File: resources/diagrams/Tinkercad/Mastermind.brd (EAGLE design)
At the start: 68.6 x 53.3 mm, 4 parts

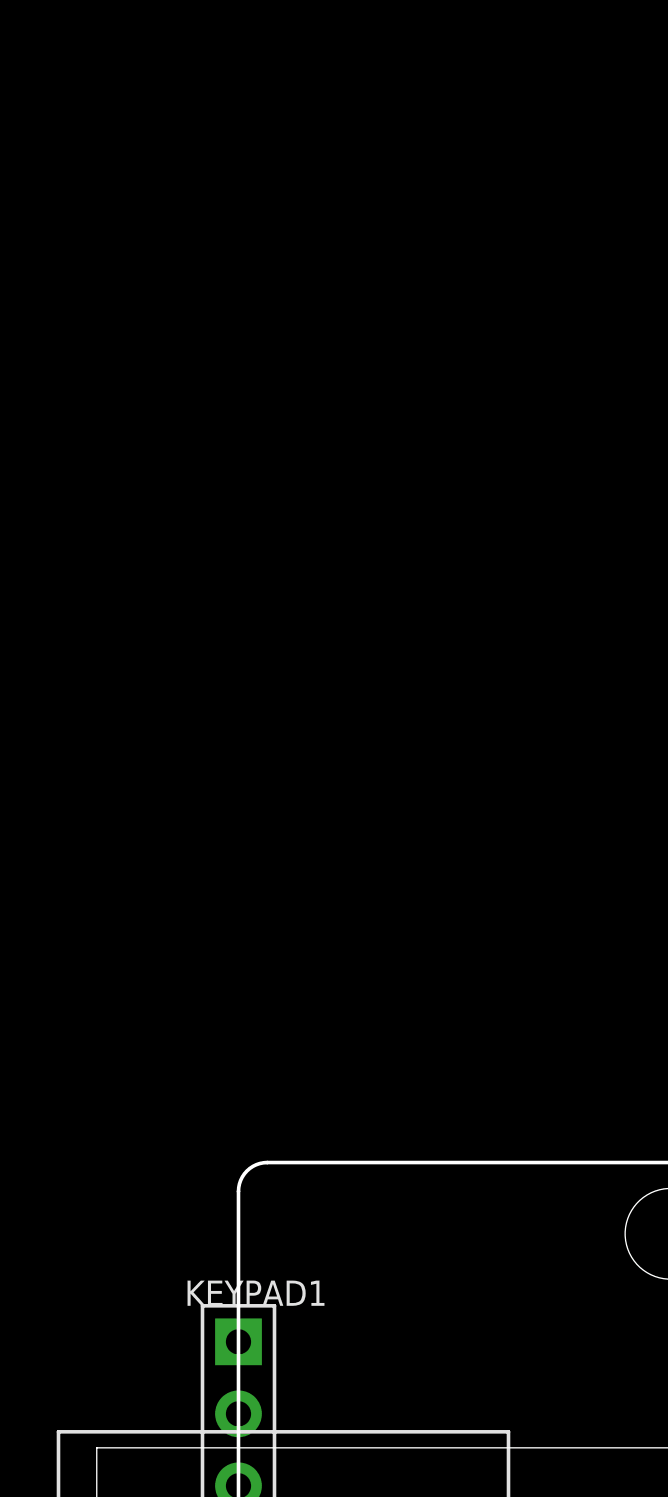
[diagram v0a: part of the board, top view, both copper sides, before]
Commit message: added LEDs
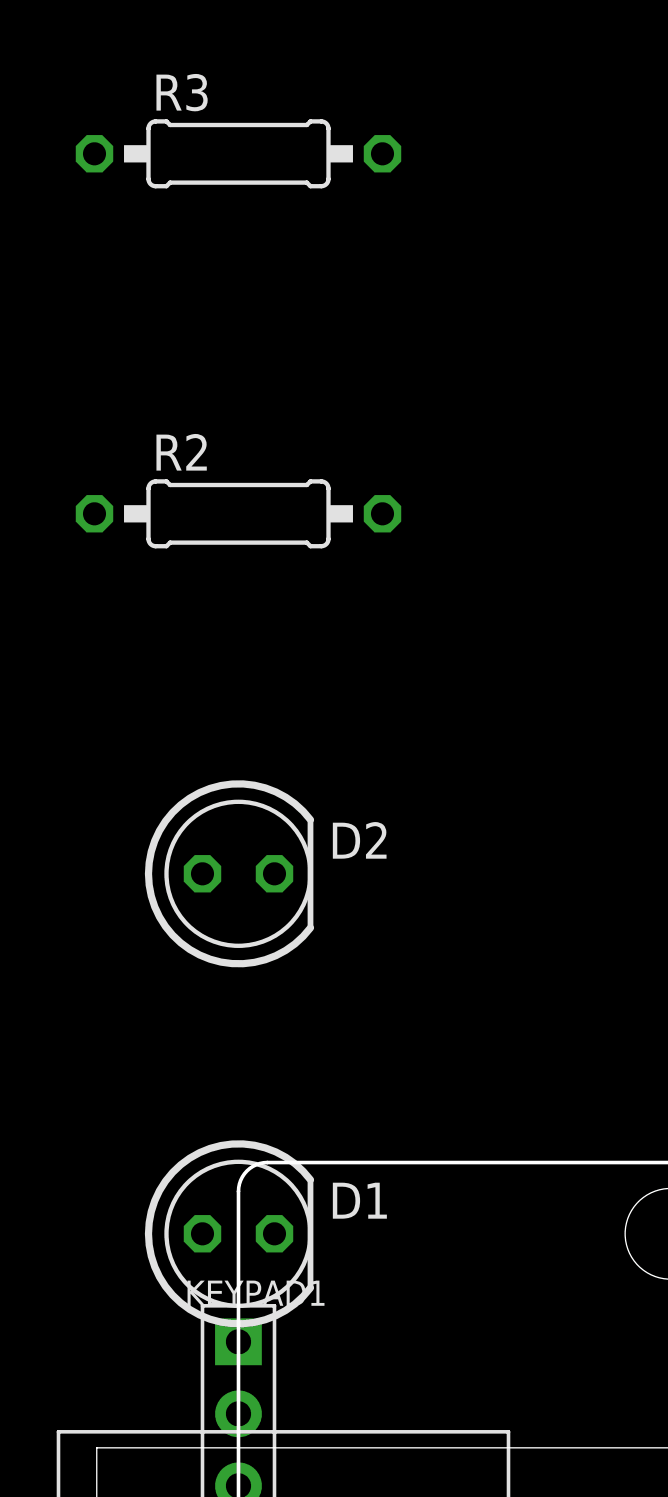
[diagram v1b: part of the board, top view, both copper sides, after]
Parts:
- added D1, D2: (no value), AUTODESK_CIRCUITS_BREADBOARD:LED5MM
- added R2, R3: 1k‎Ω, AUTODESK_CIRCUITS_BREADBOARD:0207/10
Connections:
- new net N$18: D1.K, R2.1
- new net N$19: D1.A, U1.A2
- new net N$20: D2.K, R3.1
- new net N$21: D2.A, U1.A3
- net N$16: now also R2.2, R3.2
